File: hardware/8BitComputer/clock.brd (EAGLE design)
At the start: 100 x 75 mm, 29 parts, among them IC1 LM555CN, J1 Power, J2 Power, J3 CLK_OUTS, Q1 P2N2222AZL1G, Q2 P2N2222AZL1G

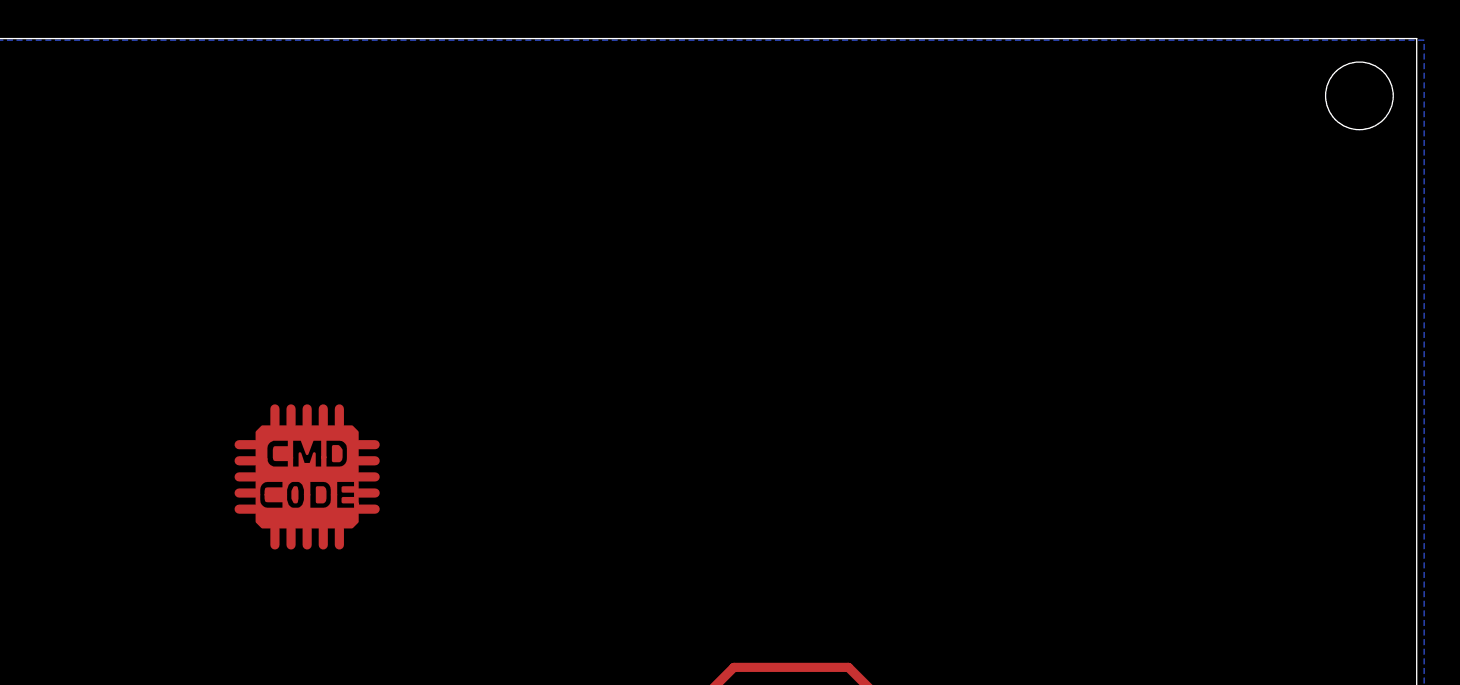
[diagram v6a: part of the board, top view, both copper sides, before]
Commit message: added holes back
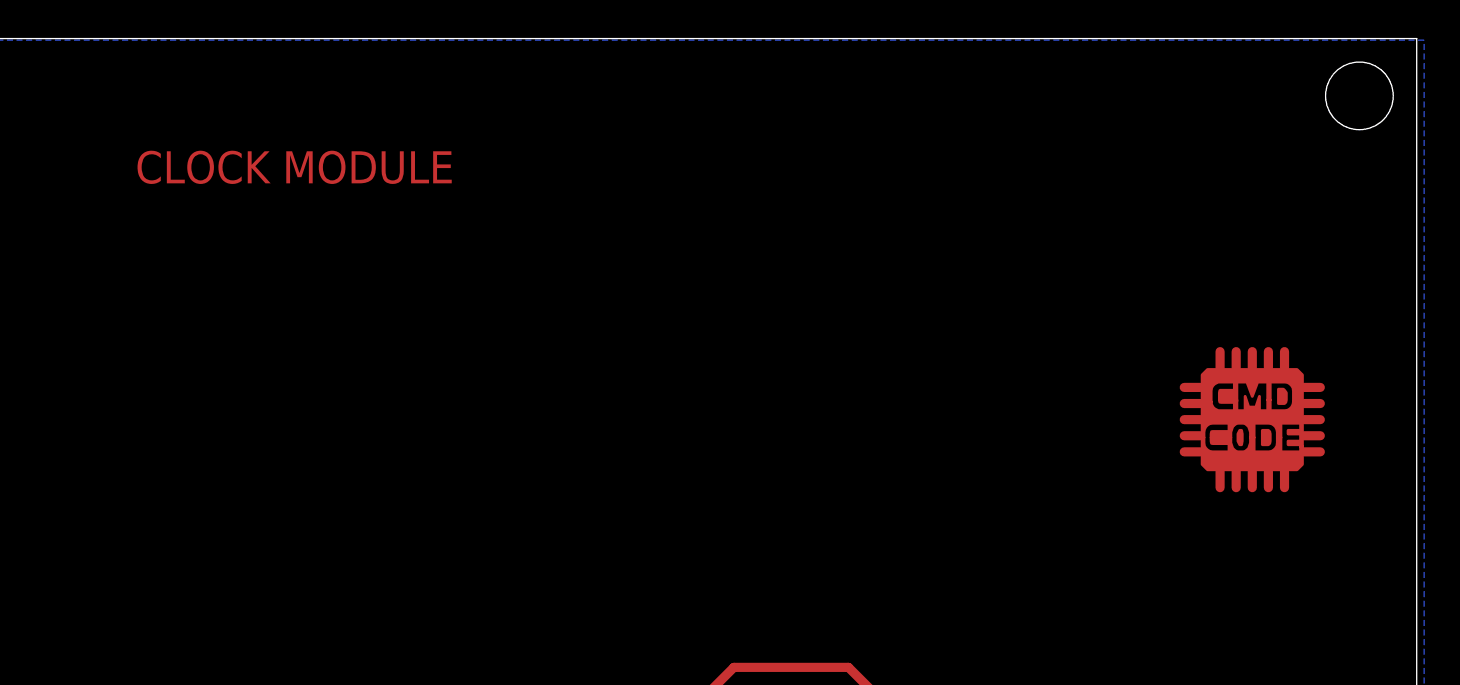
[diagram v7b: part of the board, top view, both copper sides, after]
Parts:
- moved U$3 42.0 mm to (92.7, 58.4)
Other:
- board text added: "CLOCK MODULE"
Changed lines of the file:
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@@
 <layer number="43" name="vRestrict" color="2" fill="10" visible="no" active="yes"/>
 <layer number="44" name="Drills" color="7" fill="1" visible="no" active="yes"/>
-<layer number="45" name="Holes" color="7" fill="1" visible="no" active="yes"/>
+<layer number="45" name="Holes" color="7" fill="1" visible="yes" active="yes"/>
 <layer number="46" name="Milling" color="3" fill="1" visible="no" active="yes"/>
 <layer number="47" name="Measures" color="7" fill="1" visible="no" active="yes"/>
@@
 <hole x="97.46" y="72.46" drill="3"/>
 <hole x="2.54" y="72.46" drill="3"/>
+<text x="43.18" y="68.58" size="1.4224" layer="1">CLOCK MODULE</text>
 </plain>
 <attributes>
@@
 <attribute name="VALUE" x="88.73" y="1.825" size="1.27" layer="27"/>
 </element>
-<element name="U$3" library="logos" package="CMD_C0DE_LOGO_TOP_COPPER" value="CMD_C0DE_LOGOCMD_CODE_LOGO_TOP_COPPER" x="50.8" y="55.88" smashed="yes"/>
+<element name="U$3" library="logos" package="CMD_C0DE_LOGO_TOP_COPPER" value="CMD_C0DE_LOGOCMD_CODE_LOGO_TOP_COPPER" x="92.71" y="58.42" smashed="yes"/>
 </elements>
 <signals>

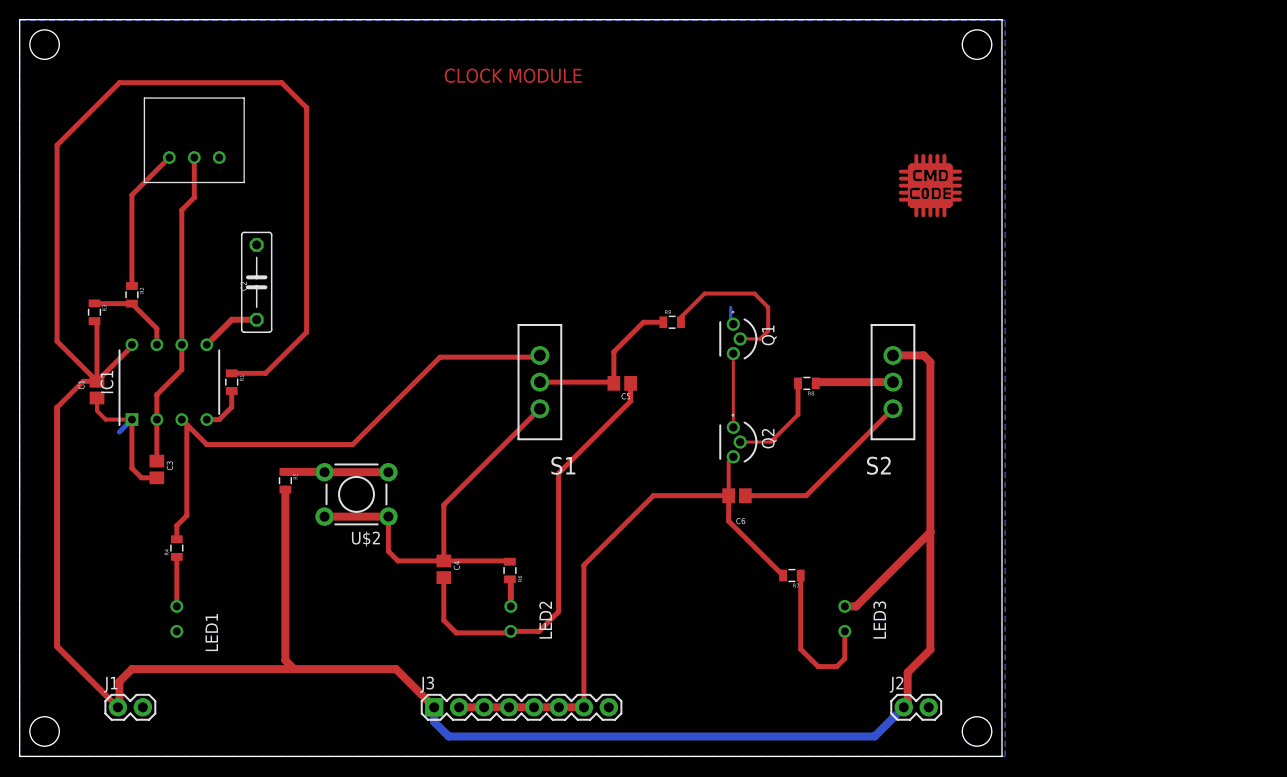
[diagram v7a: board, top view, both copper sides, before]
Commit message: updated clock to be a bit easier to solder by using bottom layer more. Thought here is that if the hole through pin only needs connection on one side then it should be the bottom so I don't have to solder both top and bottom of each pin
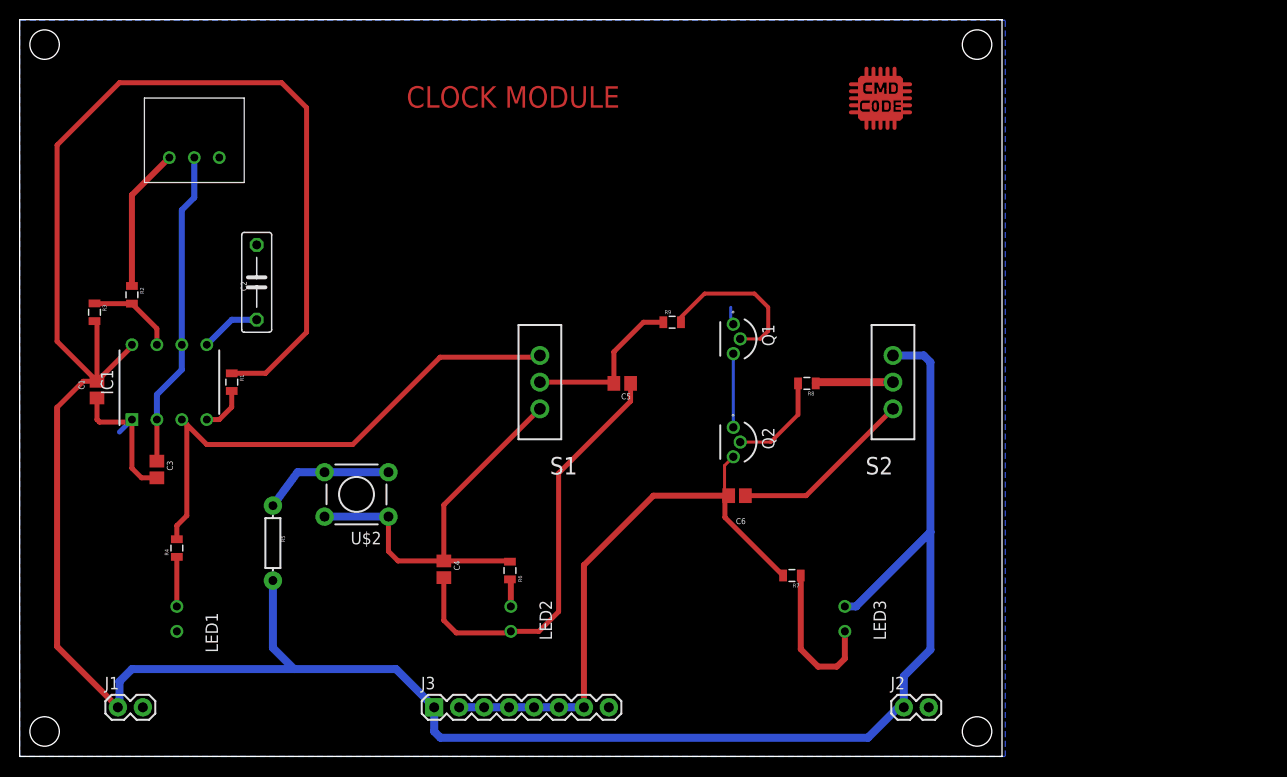
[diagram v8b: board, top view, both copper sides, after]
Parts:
- R5: device passives:0805 -> passives:AXIAL-0.3
- moved U$3 10.2 mm to (87.6, 67.3)
- moved R5 6.48 mm to (25.8, 21.7)
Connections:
- net N$6: now also R5.P$1; no longer R5.1
- net VCC5V: now also R5.P$2; no longer R5.2
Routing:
- net VCC5V: track 295.5 -> 287.5 mm
- net N$6: track 10.5 -> 13.5 mm
- net GND: track 79.2 -> 79.8 mm
